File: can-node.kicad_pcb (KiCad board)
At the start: 2 copper layers, 50 x 60 mm, 97 parts, among them P1 Debug, P2 CONN_01X04, Q1 DMP6023LSS, Q10 BSS138, Q11 BSS84P, Q12 BSS84P, Q13 BSS84P, Q14 BSS84P, Q15 BSS84P, Q3 BSS138, Q4 BSS138, Q5 BSS138, Q6 BSS138, Q7 BSS138, Q8 BSS138, Q9 BSS138, SW2 SW_PUSH, SW3 SW_PUSH, U1 LMR16006, U2 SN74LVC1G08, U3 STM32F072RB, U4 HDC1080, U5 TCAN334, X1 32.768KHz 12.5pF

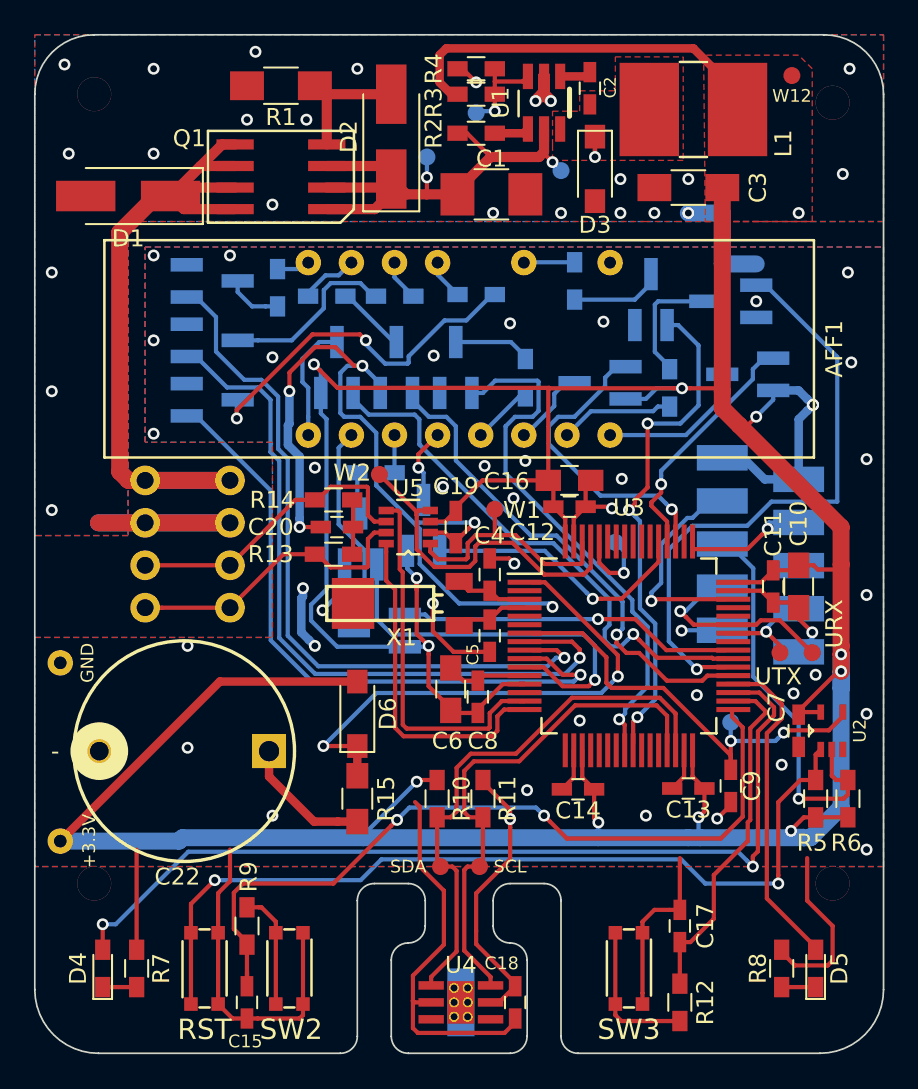
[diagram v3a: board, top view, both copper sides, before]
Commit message: Simplify over voltage protection and improve PCB.
- use new KiCad library for some parts
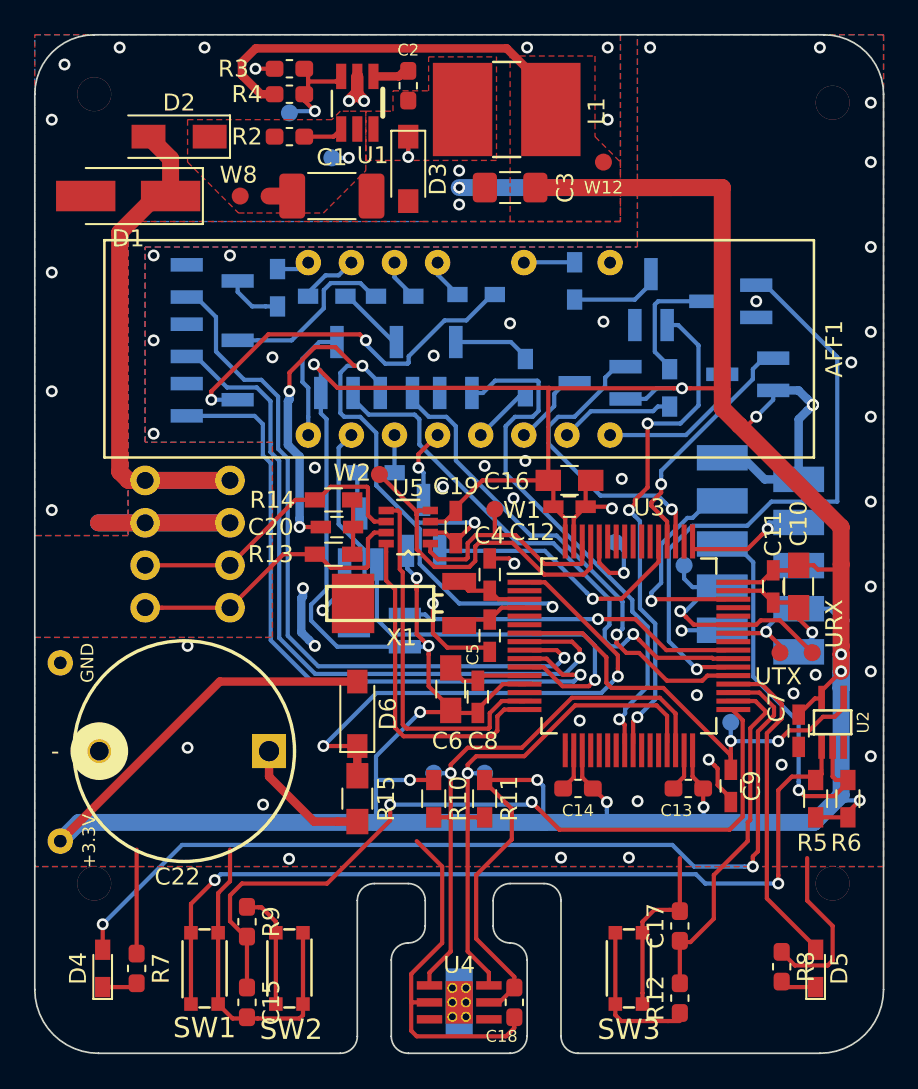
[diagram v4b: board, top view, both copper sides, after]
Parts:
- removed Q1: DMP6023LSS, can-node:DMP6023LSS
- removed R1: 100k, Resistors_SMD:R_1206_HandSoldering
- removed RST: SW_PUSH, can-node:KMR2
- removed SCL: SCL, can-node:Measurement_Point_tiny
- removed SDA: SDA, can-node:Measurement_Point_tiny
- added SW1: SW_PUSH, can-node:KMR2, F.Cu at (130.0, 120.0)
- added W16: SDA, can-node:Measurement_Point_tiny, B.Cu at (143.5, 108.5)
- added W17: SCL, can-node:Measurement_Point_tiny, B.Cu at (146.5, 108.5)
- added W4: UART_RX, can-node:Measurement_Point_tiny, B.Cu at (158.2, 96.2)
- added W5: UART_TX, can-node:Measurement_Point_tiny, B.Cu at (167.5, 99.5)
- C1: footprint Capacitors_SMD:C_1210_HandSoldering -> Capacitor_SMD:C_2010_5025Metric_Pad1.52x2.65mm_HandSolder
- C13, C14, C15, C17, C18, C2: footprint Capacitors_SMD:C_0603_HandSoldering -> Capacitor_SMD:C_0603_1608Metric_Pad1.05x0.95mm_HandSolder
- C3: footprint Capacitors_SMD:C_1206_HandSoldering -> Capacitor_SMD:C_1206_3216Metric_Pad1.42x1.75mm_HandSolder
- D2: value 10V -> 1A, 50V; footprint Diodes_SMD:D_SMA_Handsoldering -> can-node:D_SMF_Handsoldering
- R12, R2, R3, R4, R7, R8, R9: footprint Resistors_SMD:R_0603_HandSoldering -> Resistor_SMD:R_0603_1608Metric_Pad1.05x0.95mm_HandSolder
- W8: moved to F.Cu
- moved W9 13.5 mm to (137.5, 72.2)
- moved D2 12.5 mm to (128.5, 71.0), turned to 180 degrees
- moved W12 12.2 mm to (153.5, 72.5)
- moved W8 11.2 mm to (132.1, 74.5)
- moved R2 11.0 mm to (135.0, 71.0)
- moved D3 11.0 mm to (142.0, 72.9)
- moved L1 11.0 mm to (147.8, 69.4)
- moved R3 11.0 mm to (135.0, 68.5)
- moved R4 11.0 mm to (135.0, 67.0)
- moved U1 11.0 mm to (139.0, 69.0)
- moved W10 11.0 mm to (135.0, 69.6)
- moved W11 11.0 mm to (142.0, 71.0)
- moved C2 10.7 mm to (142.0, 68.0)
- moved C3 10.5 mm to (148.0, 74.0)
- moved C1 9.40 mm to (137.5, 74.5)
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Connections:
- net Net-(C1-Pad1) renamed /Power Supply/VIN
- net VBAT renamed +BATT
- D2 pad 2: Net-(D2-Pad2) -> VIN+
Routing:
- net /Power Supply/VIN: track 31.3 -> 1.86 mm, vias 2 -> 1
- net +3.3VADC: track 287.4 -> 312.4 mm
- net VIN+: track 47.9 -> 34.2 mm
- net Net-(D2-Pad2): track 8.46 -> 0.00 mm
- net GND: track 185.8 -> 194.3 mm
- net /Microcontroller/UART1_RX: track 11.6 -> 14.9 mm
- net /Microcontroller/UART1_TX: track 6.58 -> 9.37 mm
- net PC2: track 38.3 -> 40.3 mm
- net Net-(Q5-Pad3): track 21.4 -> 22.9 mm
- net Net-(R3-Pad2): track 5.72 -> 6.37 mm
- net Net-(C9-Pad1): track 26.7 -> 27.2 mm
- net Net-(R10-Pad2): track 32.0 -> 32.5 mm, vias 0 -> 1
- net Net-(R11-Pad2): track 30.5 -> 30.3 mm, vias 0 -> 1
- added copper zone on F.Cu, net /Power Supply/VIN
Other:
- net class Power 1mm added: clearance 0.5, trace_width 1, via_dia 0.7, via_drill 0.4
- board text added: "2018-07-14"
- board text added: "CAN Node Rev 1.2"
- board text removed: "2018-01-05"
- board text removed: "CAN Node Rev 1.1"

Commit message: Replace remaining parts from old KiCad library.
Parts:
- C10, C16, C6: footprint Capacitors_SMD:C_0805_HandSoldering -> Capacitor_SMD:C_0805_2012Metric_Pad1.33x1.40mm_HandSolder
- C11, C12, C19, C20, C4, C5, C7, C8, C9: footprint Capacitors_SMD:C_0603_HandSoldering -> Capacitor_SMD:C_0603_1608Metric_Pad1.05x0.95mm_HandSolder
- R10, R11, R13, R14, R25, R26, R27, R28, R33, R34, R35, R36, R5, R6: footprint Resistors_SMD:R_0603_HandSoldering -> Resistor_SMD:R_0603_1608Metric_Pad1.05x0.95mm_HandSolder
- R15: footprint Resistors_SMD:R_0805_HandSoldering -> Resistor_SMD:R_0805_2012Metric_Pad1.33x1.40mm_HandSolder
- moved X1 0.50 mm to (144.5, 98.5)
- moved C6 0.32 mm to (144.2, 103.8)
- moved R25 0.32 mm to (141.5, 80.5)
- moved R6 0.32 mm to (167.6, 109.9)
- moved R26 0.30 mm to (134.0, 79.9)
- moved C10 0.25 mm to (165.2, 97.5)
- moved R35 0.22 mm to (137.0, 80.5)
- moved R27 0.20 mm to (146.0, 80.5)
- moved C9 0.18 mm to (160.9, 109.1)
- moved C16 0.17 mm to (151.5, 91.1)
- moved R36 0.17 mm to (157.2, 85.9)
- moved R33 0.16 mm to (148.8, 85.2)
- moved R13 0.14 mm to (137.7, 95.5)
- moved R14 0.14 mm to (137.7, 92.5)
- moved C19 0.10 mm to (144.7, 94.0)
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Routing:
- net GND: track 194.3 -> 210.2 mm, vias 69 -> 80
- net Net-(R5-Pad2): track 51.8 -> 52.3 mm
